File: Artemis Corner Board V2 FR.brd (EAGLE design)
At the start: 132.4 x 63.1 mm, 91 parts, among them Q1 BSS138, U1 OPA365AIDBVR, U2 ADS1232IPWR, U3 MCP2562, U4 TM4C123GH6PMI, U5 MCP2562, U6 LM3671MF-3.3/NOPB, U8 TPS562219, U9 FT232RL, Y1 16MHz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

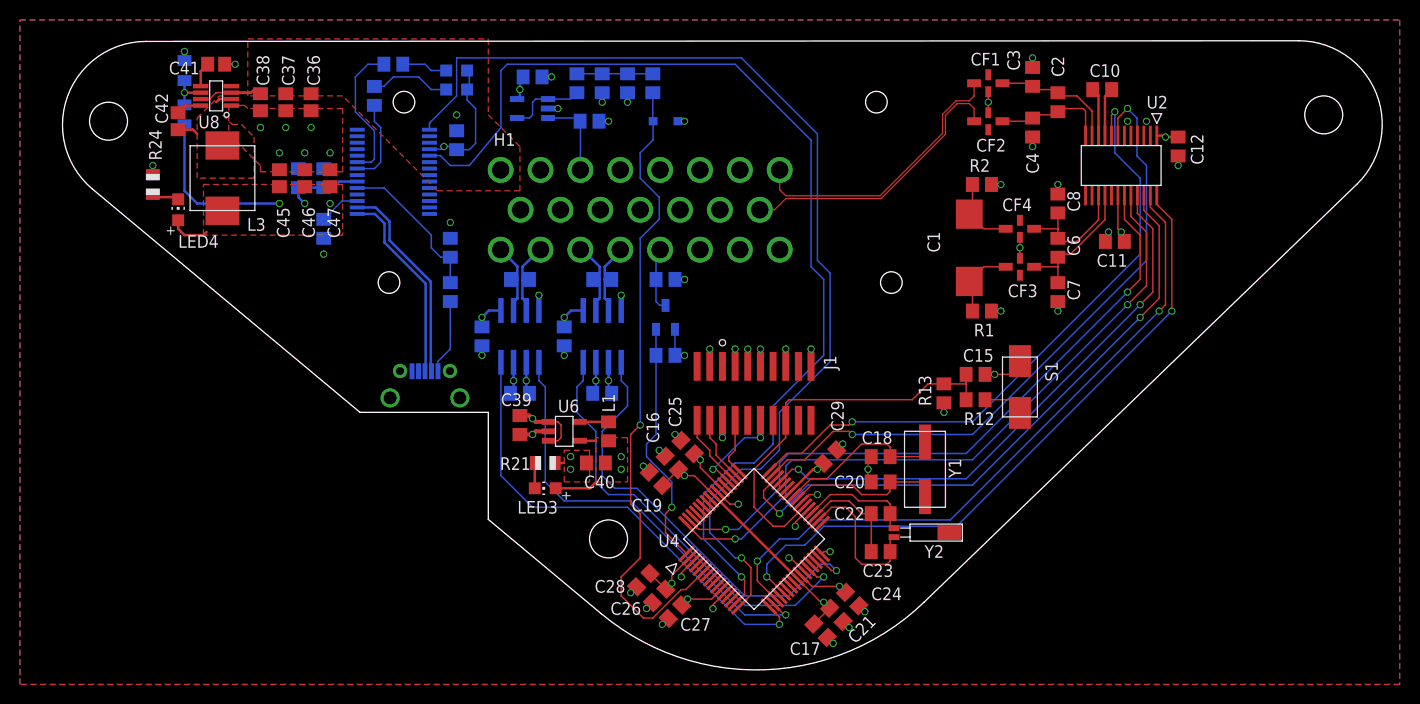
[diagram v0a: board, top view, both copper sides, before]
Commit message: ERC/DRC fixes. This still needs to be mechanically reviewed
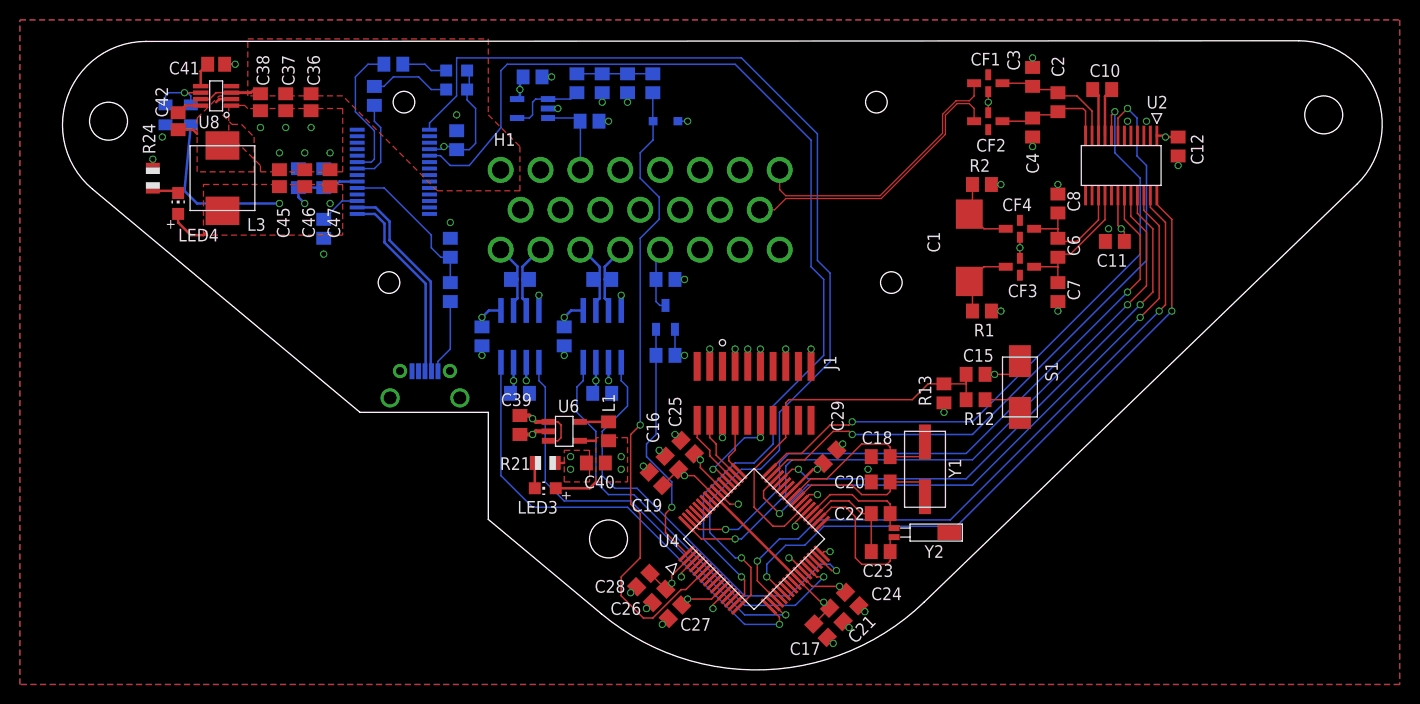
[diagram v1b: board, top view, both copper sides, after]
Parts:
- L1: value (none) -> 2.2uH
- moved R23 4.84 mm to (-39.4, 10.2), turned to 90 degrees
- moved R22 0.64 mm to (-36.8, 10.2)
- moved R24 0.64 mm to (-40.6, 3.81)
- moved LED4 0.64 mm to (-38.1, 1.27)
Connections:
- net !RESET!: now also U4.MASK-38
- net +3V3: now also U4.MASK-11, U4.MASK-2, U4.MASK-26, U4.MASK-37, U4.MASK-42, U4.MASK-54
- net ADC_!PWDN!: now also U4.MASK-46
- net ADC_CHANNEL_SELECT: now also U4.MASK-48
- net ADC_GAIN_BIT_0: now also U4.MASK-63
- net ADC_GAIN_BIT_1: now also U4.MASK-64
- net ADC_MISO: now also U4.MASK-21
- net ADC_SCLK: now also U4.MASK-19
- net ADC_SPEED: now also U4.MASK-45
- net ADC_TEMP_EN: now also U4.MASK-47
- net CAR_CAN_RX: now also U4.MASK-17
- net CAR_CAN_TX: now also U4.MASK-18
- net DAMPER_POSITION_3V3: now also U4.MASK-6
- net GND: now also U4.MASK-12, U4.MASK-27, U4.MASK-3, U4.MASK-32, U4.MASK-39, U4.MASK-55
- net N$1: now also U4.MASK-41
- net N$15: now also U4.MASK-36
- net N$17: now also U4.MASK-34
- net N$24: now also U4.MASK-35
- net N$4: now also U4.MASK-40
- net SENSOR_CAN_RX: now also U4.MASK-28
- net SENSOR_CAN_TX: now also U4.MASK-31
- net TCK: now also U4.MASK-52
- net TDI: now also U4.MASK-50
- net TDO: now also U4.MASK-49
- net TMS: now also U4.MASK-51
- net UART_RX: now also U4.MASK-16
- net UART_TX: now also U4.MASK-15
- net VDDC: now also U4.MASK-25, U4.MASK-56
- net WHEEL_TACHOMETER_3V3: now also U4.MASK-1
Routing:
- net GND: track 72.0 -> 65.8 mm
- net VFB_5V: track 4.08 -> 6.24 mm

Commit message: Fixed layout of 5v regulator
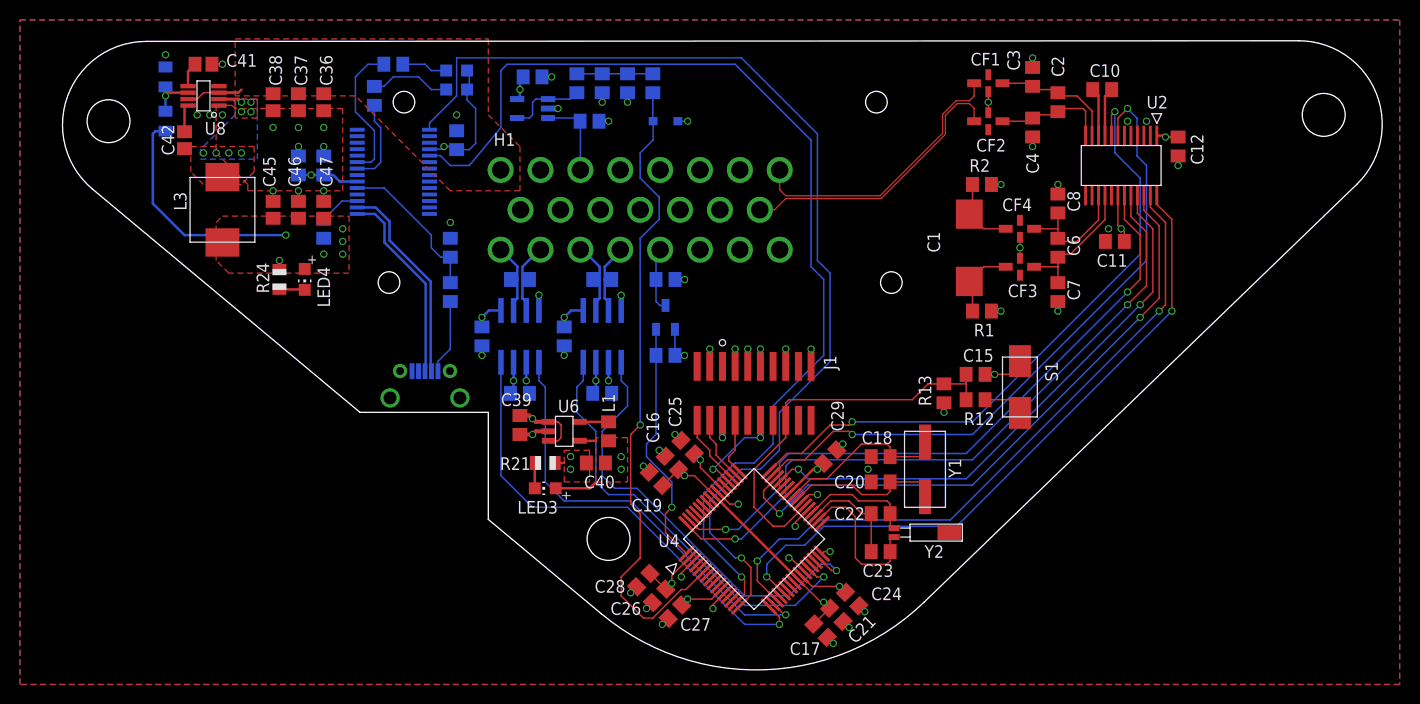
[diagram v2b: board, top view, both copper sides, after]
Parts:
- moved R24 16.3 mm to (-27.9, -6.35)
- moved LED4 14.8 mm to (-25.4, -6.35), turned to 180 degrees
- moved R23 3.81 mm to (-39.4, 14.0), turned to 270 degrees
- moved C46 3.24 mm to (-26.0, 0.64)
- moved C47 3.24 mm to (-23.5, 0.64)
- moved C45 3.24 mm to (-28.6, 0.64)
- moved L3 3.17 mm to (-33.7, 0.64)
- moved R22 2.62 mm to (-39.4, 9.53)
- moved C42 2.01 mm to (-37.5, 7.62)
- moved C41 1.27 mm to (-35.6, 15.2)
- moved U8 1.27 mm to (-35.6, 12.1)
- moved C32 1.27 mm to (-26.0, 5.08)
- moved C33 1.27 mm to (-23.5, 5.08)
- moved C36 1.27 mm to (-23.5, 11.4)
- moved C37 1.27 mm to (-26.0, 11.4)
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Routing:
- net VFB_5V: track 6.24 -> 4.84 mm
- net SW_5V: track 3.76 -> 2.39 mm, vias 0 -> 8
- net +5V: track 52.0 -> 52.1 mm, vias 10 -> 12
- net GND: vias 62 -> 67
- added copper zone on layer 16, net SW_5V
